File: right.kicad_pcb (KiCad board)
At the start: 2 copper layers, 152.4 x 109.7 mm, 42 parts, among them J1 Conn_01x07, J2 Conn_01x07, U1 74VHC4051AFT, U2 GS8051-TR

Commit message: drill
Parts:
- removed the REF** at (210.8, 157.5)
- added REF**: MountingHole_2.2mm_M2, MountingHole:MountingHole_2.2mm_M2, F.Cu at (108.0, 63.5)
- added REF**: MountingHole_2.2mm_M2, MountingHole:MountingHole_2.2mm_M2, F.Cu at (212.1, 160.0)
- added REF**: MountingHole_2.2mm_M2, MountingHole:MountingHole_2.2mm_M2, F.Cu at (119.4, 119.4)
- added REF**: MountingHole_2.2mm_M2, MountingHole:MountingHole_2.2mm_M2, F.Cu at (81.3, 139.7)
- added REF**: MountingHole_2.2mm_M2, MountingHole:MountingHole_2.2mm_M2, F.Cu at (81.3, 68.6)
- added REF**: MountingHole_2.2mm_M2, MountingHole:MountingHole_2.2mm_M2, F.Cu at (226.1, 134.6)
- added REF**: MountingHole_2.2mm_M2, MountingHole:MountingHole_2.2mm_M2, F.Cu at (209.6, 77.5)
- added REF**: MountingHole_2.2mm_M2, MountingHole:MountingHole_2.2mm_M2, F.Cu at (154.9, 97.8)
- added REF**: MountingHole_2.2mm_M2, MountingHole:MountingHole_2.2mm_M2, F.Cu at (191.8, 102.9)
- added REF**: MountingHole_2.2mm_M2, MountingHole:MountingHole_2.2mm_M2, F.Cu at (161.3, 128.3)
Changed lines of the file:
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@@
     (tracks 519)
     (zones 0)
-    (modules 42)
+    (modules 51)
     (nets 22)
   )
@@
     (add_net selb)
   )
-  (module MountingHole:MountingHole_3.5mm_Pad (layer F.Cu)
-    (at 210.82 157.48)
-    (descr "Mounting Hole 3.5mm")
-    (tags "mounting hole 3.5mm")
-    (attr virtual)
-    (fp_text reference REF** (at 0 -4.5) (layer F.SilkS)
-      (effects (font (size 1 1) (thickness 0.15)))
-    )
-    (fp_text value MountingHole_3.5mm_Pad (at 0 4.5) (layer F.Fab)
-      (effects (font (size 1 1) (thickness 0.15)))
-    )
-    (fp_circle (center 0 0) (end 3.75 0) (layer F.CrtYd) (width 0.05))
-    (fp_circle (center 0 0) (end 3.5 0) (layer Cmts.User) (width 0.15))
-    (fp_text user %R (at 0.3 0) (layer F.Fab)
-      (effects (font (size 1 1) (thickness 0.15)))
-    )
-    (pad 1 thru_hole circle (at 0 0) (size 7 7) (drill 3.5) (layers *.Cu *.Mask))
+  (module MountingHole:MountingHole_2.2mm_M2 (layer F.Cu)
+    (at 107.95 63.5)
+    (descr "Mounting Hole 2.2mm, no annular, M2")
+    (tags "mounting hole 2.2mm no annular m2")
+    (attr virtual)
+    (fp_text reference REF** (at 0 -3.2) (layer F.SilkS)
+      (effects (font (size 1 1) (thickness 0.15)))
+    )
+    (fp_text value MountingHole_2.2mm_M2 (at 0 3.2) (layer F.Fab)
+      (effects (font (size 1 1) (thickness 0.15)))
+    )
+    (fp_circle (center 0 0) (end 2.45 0) (layer F.CrtYd) (width 0.05))
+    (fp_circle (center 0 0) (end 2.2 0) (layer Cmts.User) (width 0.15))
+    (fp_text user %R (at 0.3 0) (layer F.Fab)
+      (effects (font (size 1 1) (thickness 0.15)))
+    )
+    (pad 1 np_thru_hole circle (at 0 0) (size 2.2 2.2) (drill 2.2) (layers *.Cu *.Mask))
+  )
+  (module MountingHole:MountingHole_2.2mm_M2 (layer F.Cu)
+    (at 119.38 119.38)
+    (descr "Mounting Hole 2.2mm, no annular, M2")
+    (tags "mounting hole 2.2mm no annular m2")
+    (attr virtual)
+    (fp_text reference REF** (at 0 -3.2) (layer F.SilkS)
+      (effects (font (size 1 1) (thickness 0.15)))
+    )
+    (fp_text value MountingHole_2.2mm_M2 (at 0 3.2) (layer F.Fab)
+      (effects (font (size 1 1) (thickness 0.15)))
+    )
+    (fp_circle (center 0 0) (end 2.45 0) (layer F.CrtYd) (width 0.05))
+    (fp_circle (center 0 0) (end 2.2 0) (layer Cmts.User) (width 0.15))
+    (fp_text user %R (at 0.3 0) (layer F.Fab)
+      (effects (font (size 1 1) (thickness 0.15)))
+    )
+    (pad 1 np_thru_hole circle (at 0 0) (size 2.2 2.2) (drill 2.2) (layers *.Cu *.Mask))
+  )
+  (module MountingHole:MountingHole_2.2mm_M2 (layer F.Cu)
+    (at 81.28 139.7)
+    (descr "Mounting Hole 2.2mm, no annular, M2")
+    (tags "mounting hole 2.2mm no annular m2")
+    (attr virtual)
+    (fp_text reference REF** (at 0 -3.2) (layer F.SilkS)
+      (effects (font (size 1 1) (thickness 0.15)))
+    )
+    (fp_text value MountingHole_2.2mm_M2 (at 0 3.2) (layer F.Fab)
+      (effects (font (size 1 1) (thickness 0.15)))
+    )
+    (fp_circle (center 0 0) (end 2.45 0) (layer F.CrtYd) (width 0.05))
+    (fp_circle (center 0 0) (end 2.2 0) (layer Cmts.User) (width 0.15))
+    (fp_text user %R (at 0.3 0) (layer F.Fab)
+      (effects (font (size 1 1) (thickness 0.15)))
+    )
+    (pad 1 np_thru_hole circle (at 0 0) (size 2.2 2.2) (drill 2.2) (layers *.Cu *.Mask))
+  )
+  (module MountingHole:MountingHole_2.2mm_M2 (layer F.Cu)
+    (at 81.28 68.58)
+    (descr "Mounting Hole 2.2mm, no annular, M2")
+    (tags "mounting hole 2.2mm no annular m2")
+    (attr virtual)
+    (fp_text reference REF** (at 0 -3.2) (layer F.SilkS)
+      (effects (font (size 1 1) (thickness 0.15)))
+    )
+    (fp_text value MountingHole_2.2mm_M2 (at 0 3.2) (layer F.Fab)
+      (effects (font (size 1 1) (thickness 0.15)))
+    )
+    (fp_circle (center 0 0) (end 2.45 0) (layer F.CrtYd) (width 0.05))
+    (fp_circle (center 0 0) (end 2.2 0) (layer Cmts.User) (width 0.15))
+    (fp_text user %R (at 0.3 0) (layer F.Fab)
+      (effects (font (size 1 1) (thickness 0.15)))
+    )
+    (pad 1 np_thru_hole circle (at 0 0) (size 2.2 2.2) (drill 2.2) (layers *.Cu *.Mask))
+  )
+  (module MountingHole:MountingHole_2.2mm_M2 (layer F.Cu)
+    (at 226.06 134.62)
+    (descr "Mounting Hole 2.2mm, no annular, M2")
+    (tags "mounting hole 2.2mm no annular m2")
+    (attr virtual)
+    (fp_text reference REF** (at 0 -3.2) (layer F.SilkS)
+      (effects (font (size 1 1) (thickness 0.15)))
+    )
+    (fp_text value MountingHole_2.2mm_M2 (at 0 3.2) (layer F.Fab)
+      (effects (font (size 1 1) (thickness 0.15)))
+    )
+    (fp_circle (center 0 0) (end 2.45 0) (layer F.CrtYd) (width 0.05))
+    (fp_circle (center 0 0) (end 2.2 0) (layer Cmts.User) (width 0.15))
+    (fp_text user %R (at 0.3 0) (layer F.Fab)
+      (effects (font (size 1 1) (thickness 0.15)))
+    )
+    (pad 1 np_thru_hole circle (at 0 0) (size 2.2 2.2) (drill 2.2) (layers *.Cu *.Mask))
+  )
+  (module MountingHole:MountingHole_2.2mm_M2 (layer F.Cu)
+    (at 209.55 77.47)
+    (descr "Mounting Hole 2.2mm, no annular, M2")
+    (tags "mounting hole 2.2mm no annular m2")
+    (attr virtual)
+    (fp_text reference REF** (at 0 -3.2) (layer F.SilkS)
+      (effects (font (size 1 1) (thickness 0.15)))
+    )
+    (fp_text value MountingHole_2.2mm_M2 (at 0 3.2) (layer F.Fab)
+      (effects (font (size 1 1) (thickness 0.15)))
+    )
+    (fp_circle (center 0 0) (end 2.45 0) (layer F.CrtYd) (width 0.05))
+    (fp_circle (center 0 0) (end 2.2 0) (layer Cmts.User) (width 0.15))
+    (fp_text user %R (at 0.3 0) (layer F.Fab)
+      (effects (font (size 1 1) (thickness 0.15)))
+    )
+    (pad 1 np_thru_hole circle (at 0 0) (size 2.2 2.2) (drill 2.2) (layers *.Cu *.Mask))
+  )
+  (module MountingHole:MountingHole_2.2mm_M2 (layer F.Cu)
+    (at 154.94 97.79)
+    (descr "Mounting Hole 2.2mm, no annular, M2")
+    (tags "mounting hole 2.2mm no annular m2")
+    (attr virtual)
+    (fp_text reference REF** (at 0 -3.2) (layer F.SilkS)
+      (effects (font (size 1 1) (thickness 0.15)))
+    )
+    (fp_text value MountingHole_2.2mm_M2 (at 0 3.2) (layer F.Fab)
+      (effects (font (size 1 1) (thickness 0.15)))
+    )
+    (fp_circle (center 0 0) (end 2.45 0) (layer F.CrtYd) (width 0.05))
+    (fp_circle (center 0 0) (end 2.2 0) (layer Cmts.User) (width 0.15))
+    (fp_text user %R (at 0.3 0) (layer F.Fab)
+      (effects (font (size 1 1) (thickness 0.15)))
+    )
+    (pad 1 np_thru_hole circle (at 0 0) (size 2.2 2.2) (drill 2.2) (layers *.Cu *.Mask))
+  )
+  (module MountingHole:MountingHole_2.2mm_M2 (layer F.Cu)
+    (at 191.77 102.87)
+    (descr "Mounting Hole 2.2mm, no annular, M2")
+    (tags "mounting hole 2.2mm no annular m2")
+    (attr virtual)
+    (fp_text reference REF** (at 0 -3.2) (layer F.SilkS)
+      (effects (font (size 1 1) (thickness 0.15)))
+    )
+    (fp_text value MountingHole_2.2mm_M2 (at 0 3.2) (layer F.Fab)
+      (effects (font (size 1 1) (thickness 0.15)))
+    )
+    (fp_circle (center 0 0) (end 2.45 0) (layer F.CrtYd) (width 0.05))
+    (fp_circle (center 0 0) (end 2.2 0) (layer Cmts.User) (width 0.15))
+    (fp_text user %R (at 0.3 0) (layer F.Fab)
+      (effects (font (size 1 1) (thickness 0.15)))
+    )
+    (pad 1 np_thru_hole circle (at 0 0) (size 2.2 2.2) (drill 2.2) (layers *.Cu *.Mask))
+  )
+  (module MountingHole:MountingHole_2.2mm_M2 (layer F.Cu)
+    (at 161.29 128.27)
+    (descr "Mounting Hole 2.2mm, no annular, M2")
+    (tags "mounting hole 2.2mm no annular m2")
+    (attr virtual)
+    (fp_text reference REF** (at 0 -3.2) (layer F.SilkS)
+      (effects (font (size 1 1) (thickness 0.15)))
+    )
+    (fp_text value MountingHole_2.2mm_M2 (at 0 3.2) (layer F.Fab)
+      (effects (font (size 1 1) (thickness 0.15)))
+    )
+    (fp_circle (center 0 0) (end 2.45 0) (layer F.CrtYd) (width 0.05))
+    (fp_circle (center 0 0) (end 2.2 0) (layer Cmts.User) (width 0.15))
+    (fp_text user %R (at 0.3 0) (layer F.Fab)
+      (effects (font (size 1 1) (thickness 0.15)))
+    )
+    (pad 1 np_thru_hole circle (at 0 0) (size 2.2 2.2) (drill 2.2) (layers *.Cu *.Mask))
+  )
+  (module MountingHole:MountingHole_2.2mm_M2 (layer F.Cu)
+    (at 212.09 160.02)
+    (descr "Mounting Hole 2.2mm, no annular, M2")
+    (tags "mounting hole 2.2mm no annular m2")
+    (attr virtual)
+    (fp_text reference REF** (at 0 -3.2) (layer F.SilkS)
+      (effects (font (size 1 1) (thickness 0.15)))
+    )
+    (fp_text value MountingHole_2.2mm_M2 (at 0 3.2) (layer F.Fab)
+      (effects (font (size 1 1) (thickness 0.15)))
+    )
+    (fp_circle (center 0 0) (end 2.45 0) (layer F.CrtYd) (width 0.05))
+    (fp_circle (center 0 0) (end 2.2 0) (layer Cmts.User) (width 0.15))
+    (fp_text user %R (at 0.3 0) (layer F.Fab)
+      (effects (font (size 1 1) (thickness 0.15)))
+    )
+    (pad 1 np_thru_hole circle (at 0 0) (size 2.2 2.2) (drill 2.2) (layers *.Cu *.Mask))
   )
   (module lib:SOT-23-5 (layer F.Cu)

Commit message: fix
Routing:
- net col6: track 112.9 -> 119.7 mm
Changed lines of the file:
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@@
     (thickness 1.6)
     (drawings 35)
-    (tracks 519)
+    (tracks 521)
     (zones 0)
     (modules 51)
@@
   (segment (start 202.034025 125.976) (end 214.734025 138.676) (width 0.254) (layer F.Cu) (net 3))
   (segment (start 203.438 84.836) (end 203.438 77.486) (width 0.254) (layer F.Cu) (net 3))
-  (segment (start 203.438 77.486) (end 191.738 65.786) (width 0.254) (layer F.Cu) (net 3))
   (segment (start 191.738 65.786) (end 182.118 65.786) (width 0.254) (layer F.Cu) (net 3))
   (segment (start 174.498 58.166) (end 170.688 58.166) (width 0.254) (layer F.Cu) (net 3))
   (segment (start 182.118 65.786) (end 174.498 58.166) (width 0.254) (layer F.Cu) (net 3))
+  (segment (start 191.738 65.786) (end 191.738 77.438) (width 0.254) (layer F.Cu) (net 3))
+  (segment (start 191.786 77.486) (end 203.438 77.486) (width 0.254) (layer F.Cu) (net 3))
+  (segment (start 191.738 77.438) (end 191.786 77.486) (width 0.254) (layer F.Cu) (net 3))
   (via (at 184.769036 81.378982) (size 0.8) (drill 0.4) (layers F.Cu B.Cu) (net 4))
   (segment (start 184.388 74.676) (end 184.388 80.997946) (width 0.254) (layer F.Cu) (net 4))

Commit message: add zone
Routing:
- added copper zone on B.Cu, net GND
- added copper zone on F.Cu, net GND

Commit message: clean up & add script
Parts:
- TP1, TP10, TP11, TP12, TP13, TP14, TP15, TP16, TP17, TP18, TP19, TP2, TP20, TP21, TP22, TP23, TP24, TP25, TP26, TP27, TP28, TP3, TP4, TP5, TP6, TP7, TP8, TP9: footprint lib:ToprePad -> base:ToprePad
- U1: footprint gsg-modules:TSSOP16 -> base:TSSOP16

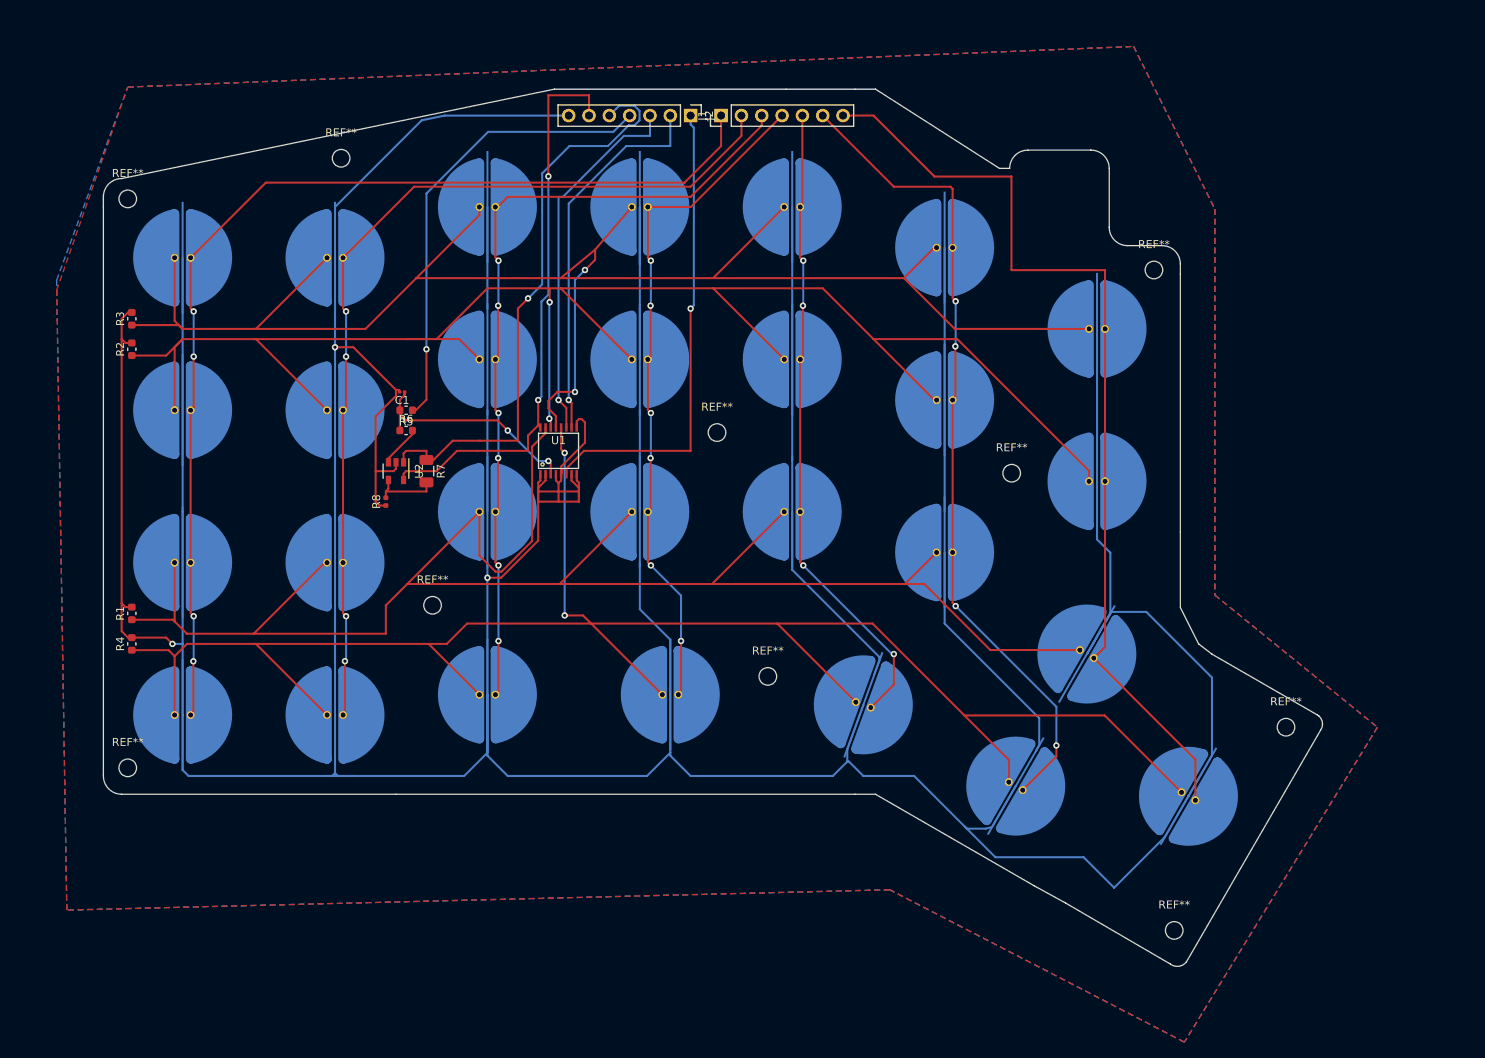
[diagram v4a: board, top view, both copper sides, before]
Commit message: 3d -> 2d
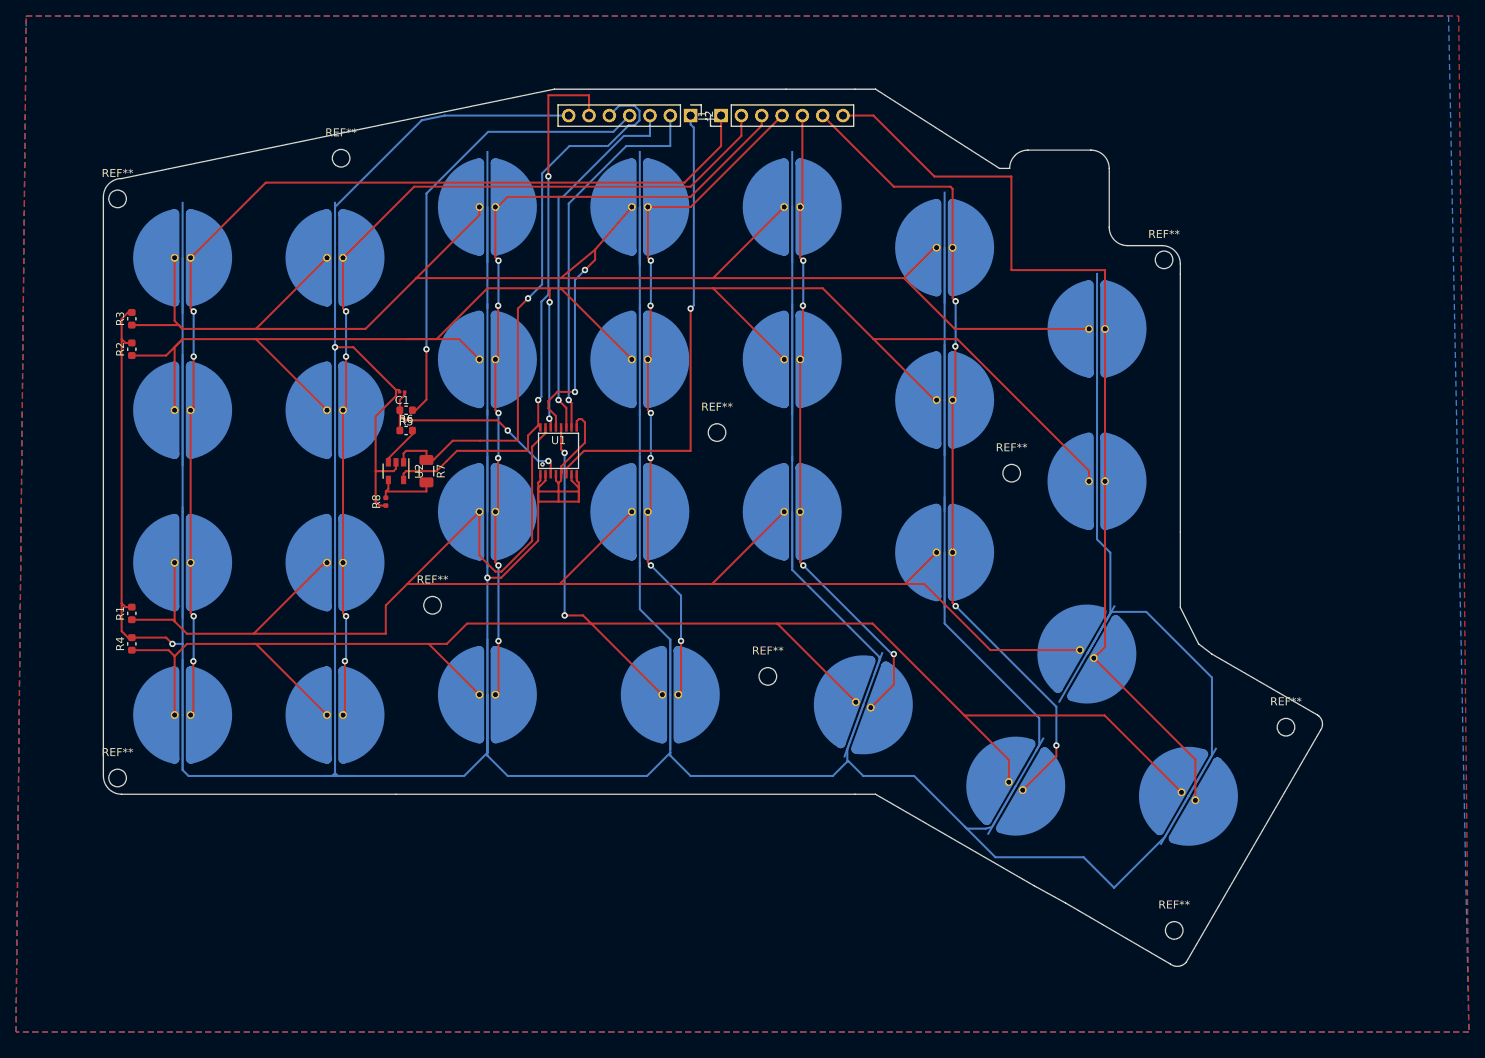
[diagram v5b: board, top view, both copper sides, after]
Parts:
- moved REF** 1.80 mm to (80.0, 141.0)
- moved REF** 1.80 mm to (210.8, 76.2)
- moved REF** 1.27 mm to (80.0, 68.6)
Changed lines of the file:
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@@
   )
   (module MountingHole:MountingHole_2.2mm_M2 (layer F.Cu)
-    (at 81.28 139.7)
+    (at 80.01 140.97)
     (descr "Mounting Hole 2.2mm, no annular, M2")
     (tags "mounting hole 2.2mm no annular m2")
@@
   )
   (module MountingHole:MountingHole_2.2mm_M2 (layer F.Cu)
-    (at 81.28 68.58)
+    (at 80.01 68.58)
     (descr "Mounting Hole 2.2mm, no annular, M2")
     (tags "mounting hole 2.2mm no annular m2")
@@
   )
   (module MountingHole:MountingHole_2.2mm_M2 (layer F.Cu)
-    (at 209.55 77.47)
+    (at 210.82 76.2)
     (descr "Mounting Hole 2.2mm, no annular, M2")
     (tags "mounting hole 2.2mm no annular m2")
@@
   (segment (start 133.858 65.76699) (end 133.858 80.555998) (width 0.254) (layer B.Cu) (net 21))
   (segment (start 133.858 80.555998) (end 132.987999 81.425999) (width 0.254) (layer B.Cu) (net 21))
+  (zone (net 1) (net_name GND) (layer B.Cu) (hatch edge 0.508)
+    (connect_pads (clearance 0.508))
+    (min_thickness 0.254)
+    (fill yes (arc_segments 32) (thermal_gap 0.508) (thermal_bridge_width 0.508))
+    (polygon
+      (pts
+        (xy 248.92 172.72) (xy 67.31 172.72) (xy 68.58 46.99) (xy 68.58 45.72) (xy 246.38 45.72)
+      )
+    )
+  )
   (zone (net 1) (net_name GND) (layer F.Cu) (hatch edge 0.508)
     (connect_pads (clearance 0.508))
@@
     (polygon
       (pts
-        (xy 217.17 69.85) (xy 217.17 118.11) (xy 237.49 134.62) (xy 213.36 173.99) (xy 176.53 154.94)
-        (xy 73.66 157.48) (xy 72.39 80.01) (xy 81.28 54.61) (xy 207.01 49.53)
+        (xy 248.92 172.72) (xy 67.31 172.72) (xy 68.58 45.72) (xy 247.65 45.72)
       )
     )
-  )
-  (zone (net 1) (net_name GND) (layer B.Cu) (hatch edge 0.508)
-    (connect_pads (clearance 0.508))
-    (min_thickness 0.254)
-    (fill yes (arc_segments 32) (thermal_gap 0.508) (thermal_bridge_width 0.508))
-    (polygon
-      (pts
-        (xy 217.17 69.85) (xy 217.17 118.11) (xy 237.49 134.62) (xy 213.36 173.99) (xy 176.53 154.94)
-        (xy 73.66 157.48) (xy 72.39 78.74) (xy 81.28 54.61) (xy 207.01 49.53)
-      )
-    )

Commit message: clean up
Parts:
- removed J1, J2: Conn_01x07, Connector_PinHeader_2.54mm:PinHeader_1x07_P2.54mm_Vertical
- removed REF** (x10): MountingHole_2.2mm_M2, MountingHole:MountingHole_2.2mm_M2
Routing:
- net GND: track 776.9 -> 0.00 mm, vias 3 -> 0
- net col0: track 133.7 -> 0.00 mm, vias 4 -> 0
- net col6: track 119.7 -> 0.00 mm
- net col1: track 116.4 -> 0.00 mm, vias 4 -> 0
- net col5: track 102.6 -> 0.00 mm, vias 4 -> 0
- net col2: track 100.4 -> 0.00 mm, vias 6 -> 0
- net row0: track 216.6 -> 131.4 mm, vias 2 -> 1
- net col3: track 85.0 -> 0.00 mm, vias 6 -> 0
- net col4: track 80.6 -> 0.00 mm, vias 4 -> 0
- net read: track 73.0 -> 0.00 mm, vias 1 -> 0
- net +5V: track 71.0 -> 0.00 mm, vias 2 -> 0
- net inh: track 59.4 -> 0.00 mm, vias 1 -> 0
- net drain: track 57.5 -> 0.00 mm, vias 1 -> 0
- net selb: track 47.6 -> 0.00 mm, vias 1 -> 0
- net sela: track 46.4 -> 0.00 mm, vias 1 -> 0
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- removed copper zone on B.Cu, net GND
- removed copper zone on F.Cu, net GND
